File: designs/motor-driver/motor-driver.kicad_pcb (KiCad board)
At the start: 2 copper layers, 48.3 x 48.3 mm, 36 parts, among them IC1 ATMEGA168-P, P1 BATT, P2 ISP, P3 MOTOR_1, P4 MOTOR_2, P5 MOTOR_3, P6 MOTOR_4, P7 CONN_7, U1 L293D, U2 L293D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

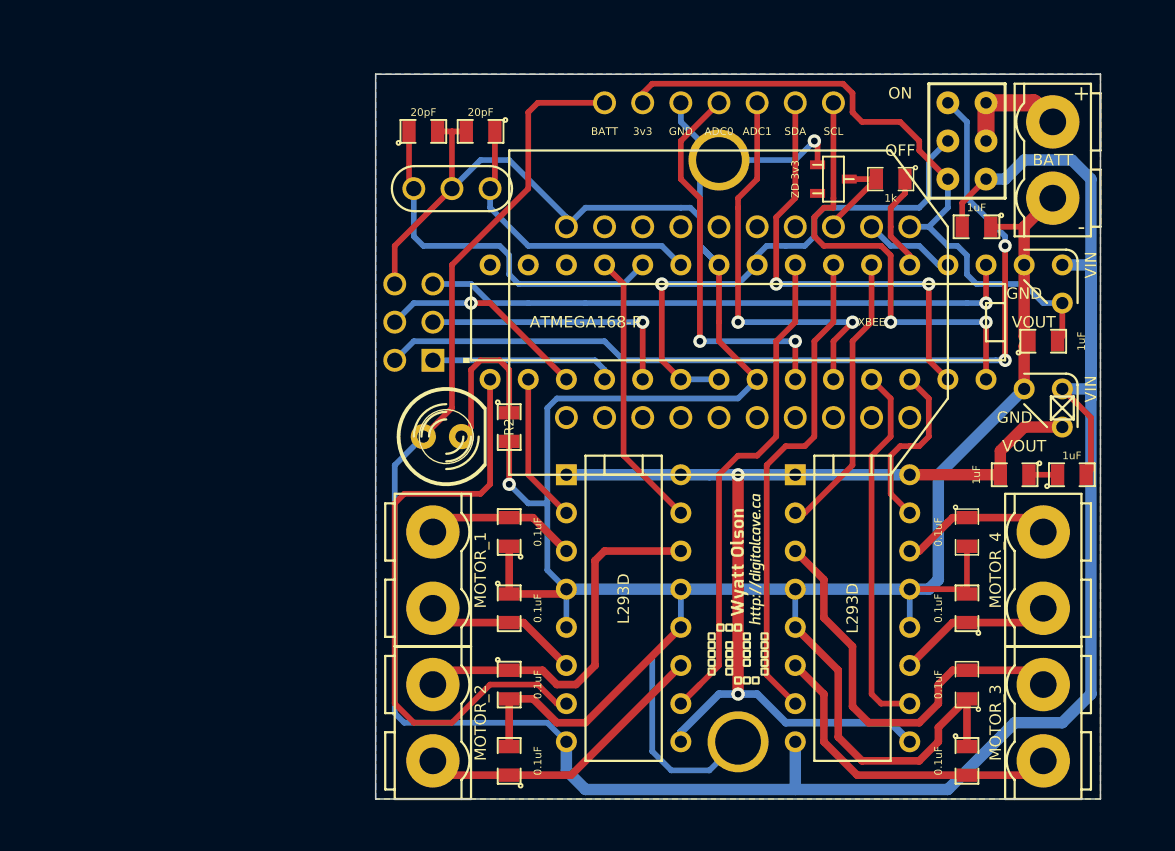
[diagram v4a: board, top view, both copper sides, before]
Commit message: Added some more caps on +5, +BATT, and AVR_VCC
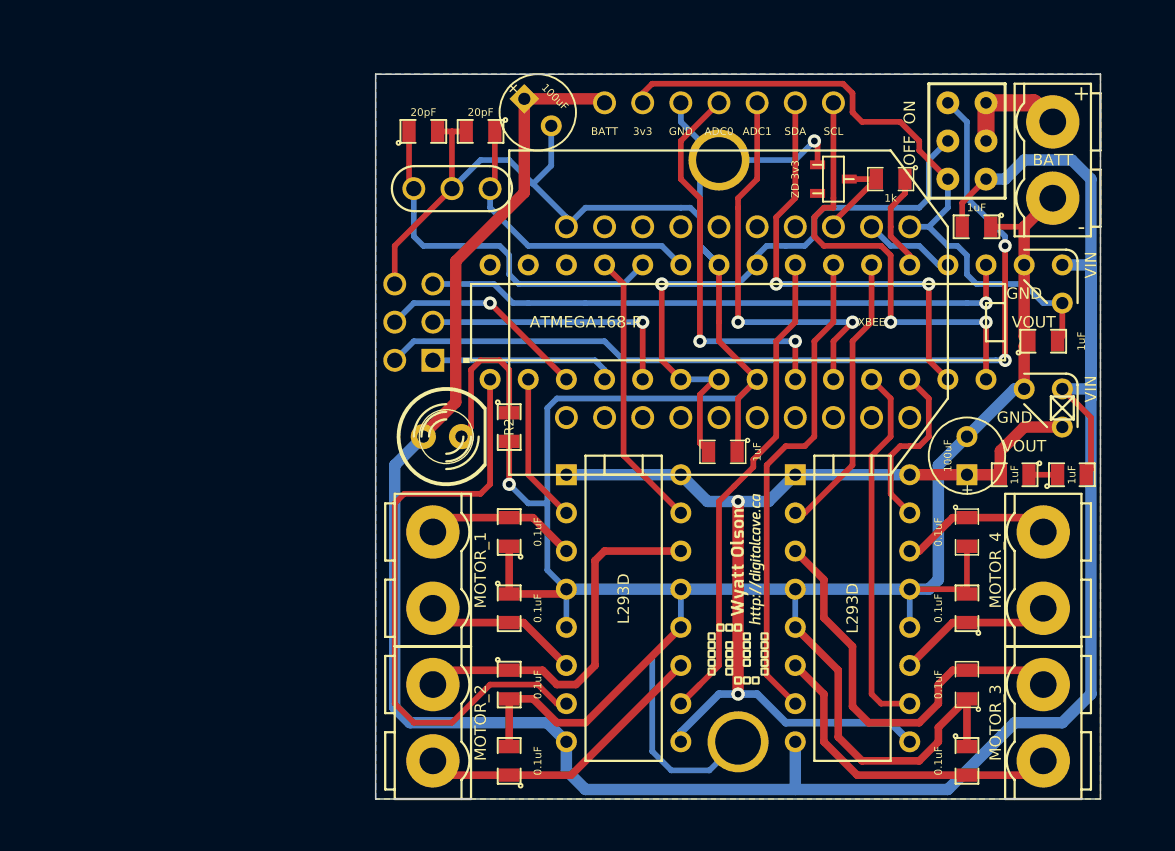
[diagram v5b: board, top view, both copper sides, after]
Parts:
- added C15: 100uF, C1V5, F.Cu at (42.5, 38.1)
- added C16: 100uF, C1V5, F.Cu at (71.1, 61.0)
- added C17: 1uF, SM0805, F.Cu at (54.9, 60.7)
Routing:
- net GND: track 243.2 -> 253.3 mm
- net /AVR_VCC: track 35.0 -> 40.8 mm
- net /MOTOR2_3A: track 36.7 -> 36.0 mm
- net +BATT: track 169.9 -> 170.6 mm
